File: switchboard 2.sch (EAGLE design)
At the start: 217 parts, among them IC1 MT8816AP, IC10 Z8F2480SO, IC11 LMV321M5, IC12 74HC595D, IC14 74LVC1G125DBV, IC15 74LVC1G125DBV, IC16 LM2940-9, IC17 PC817S OPTO, IC2 NE5532D, IC3 TC7660-SOIC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

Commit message: Polarity inversion protection diode added to -5V. USB ESD protection connection changed from GND to USB shield. Layout development and changes to improve performance, considering current loops.
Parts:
- added D20: LL4148, diode:DIODE-MINIMELF
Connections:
- net -5V: now also D20.A
- net GND: now also D20.C, H1.MOUNT, H2.MOUNT, H3.MOUNT; no longer D19.GND
- net USB_SHLD: now also D19.GND
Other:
- note added: "3.3V regulator as a option when FT232 (and its regulator) is not mounted or not used."
- note added: "Vin máx = 25 V"
- note removed: "3.3V regulator as a option when FT232 (and its regulator) is not mounted."
- moved on the sheet: C21, L1, SJ2

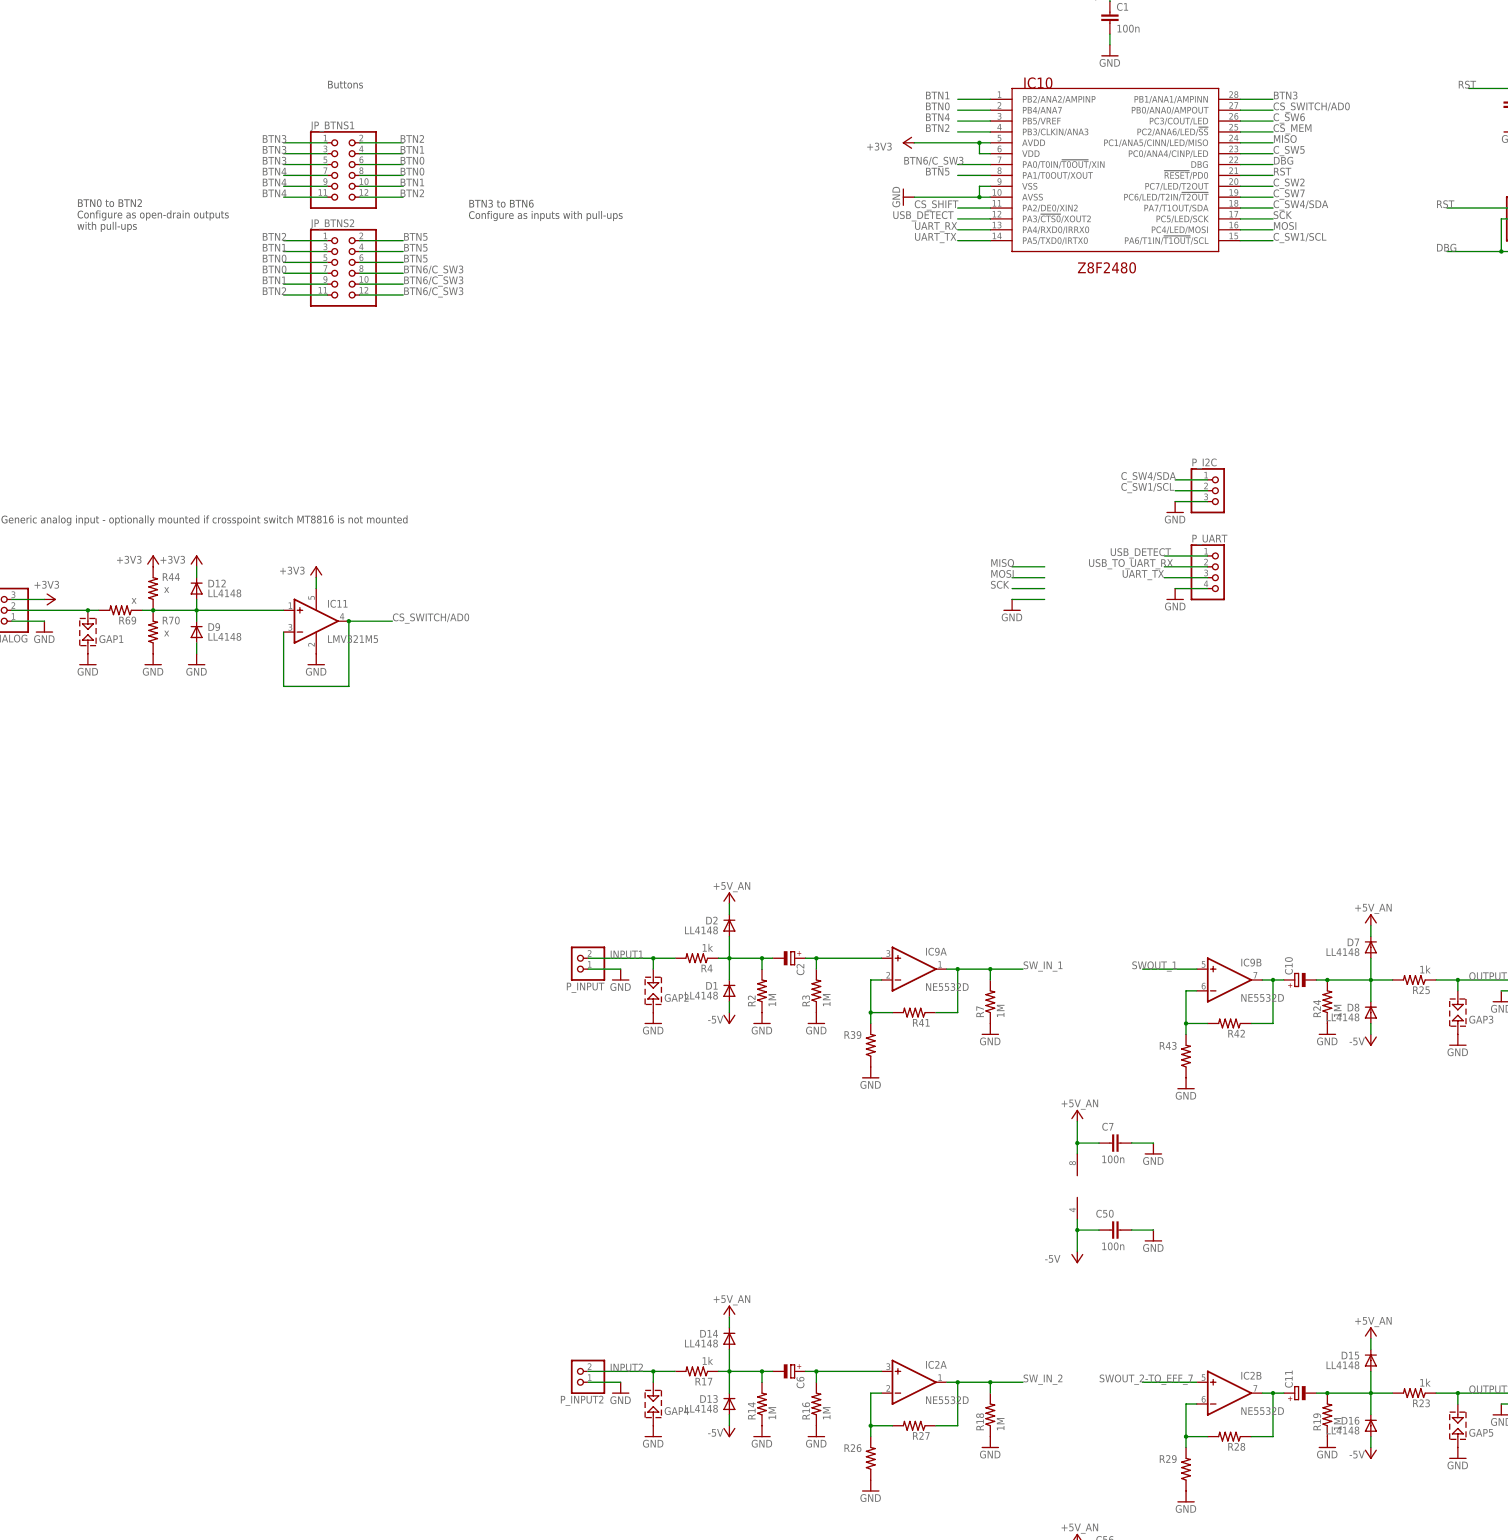
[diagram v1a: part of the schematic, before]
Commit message: Final adjustments to the schematic and layout. Cap added close to the generic input opamp. RC filter against EMI added to the audio inputs. Bias resistors added to output opamps.
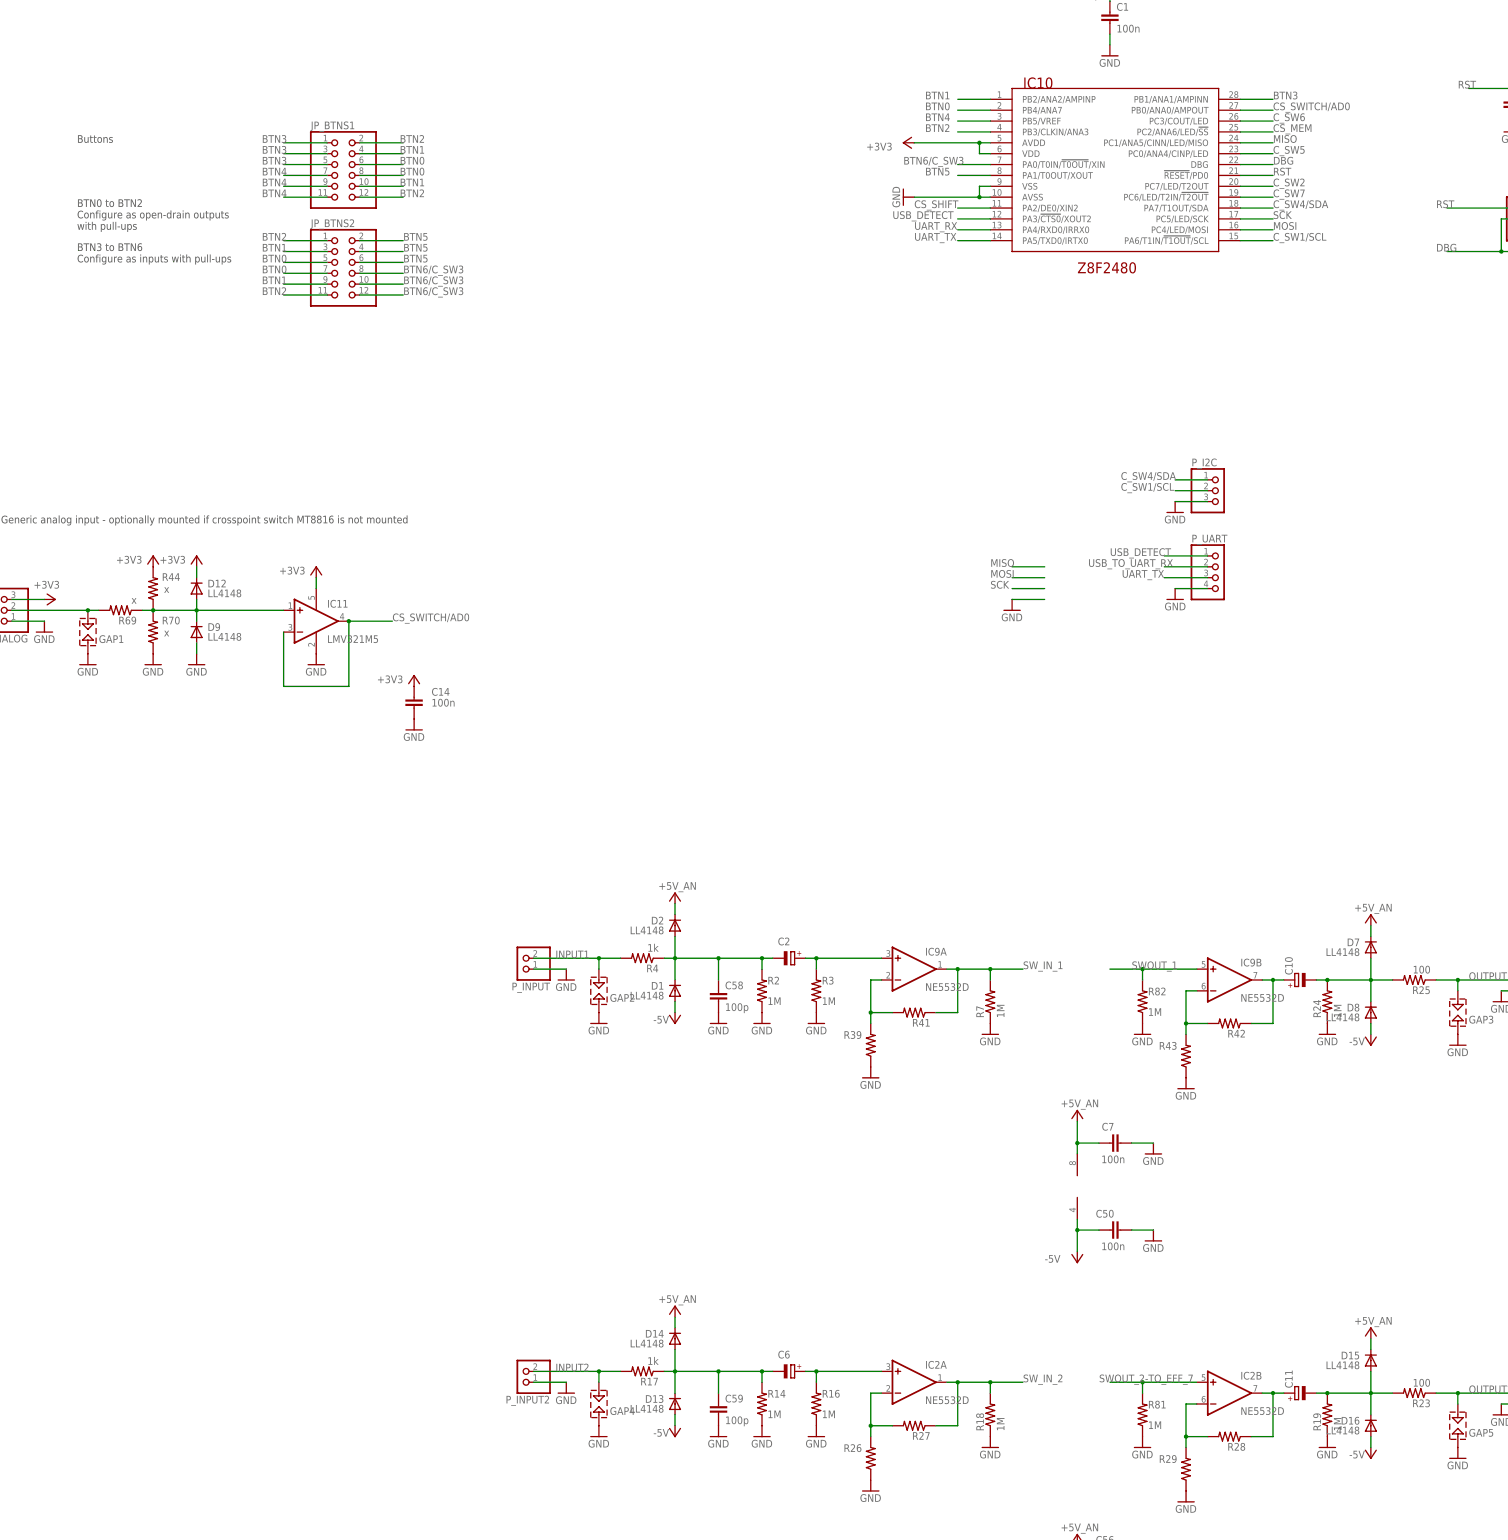
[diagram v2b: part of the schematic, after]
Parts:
- added C14: 100n, rcl:C-EUC0603
- added C58, C59: 100p, rcl:C-EUC0603
- added R81, R82: 1M, rcl:R-US_R0603
- R23, R25: value 1k -> 100
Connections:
- net +3V3: now also C14.1
- net GND: now also C14.2, C58.2, C59.2, R81.1, R82.1
- net N$4: now also C58.1
- net N$54: now also C59.1
- net SWOUT_1: now also R82.2
- net SWOUT_2-TO_EFF_7: now also R81.2
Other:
- moved on the sheet: D1, D13, D14, D2, GAP2, GAP4, P_INPUT, P_INPUT2, R17, R4

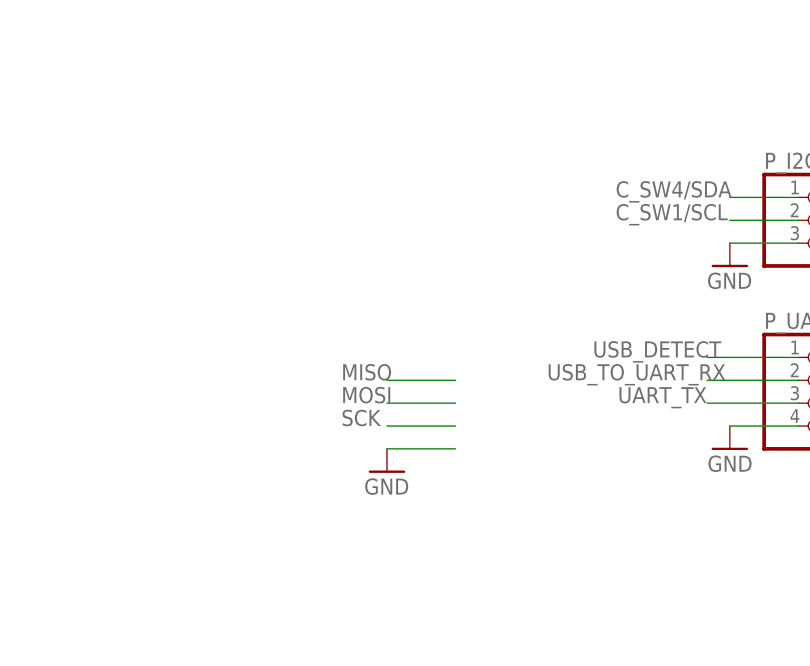
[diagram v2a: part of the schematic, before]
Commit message: Final adjustments. Test points added to SPI and supplies. PTSK Engineering text added (in solder mask stop layer).
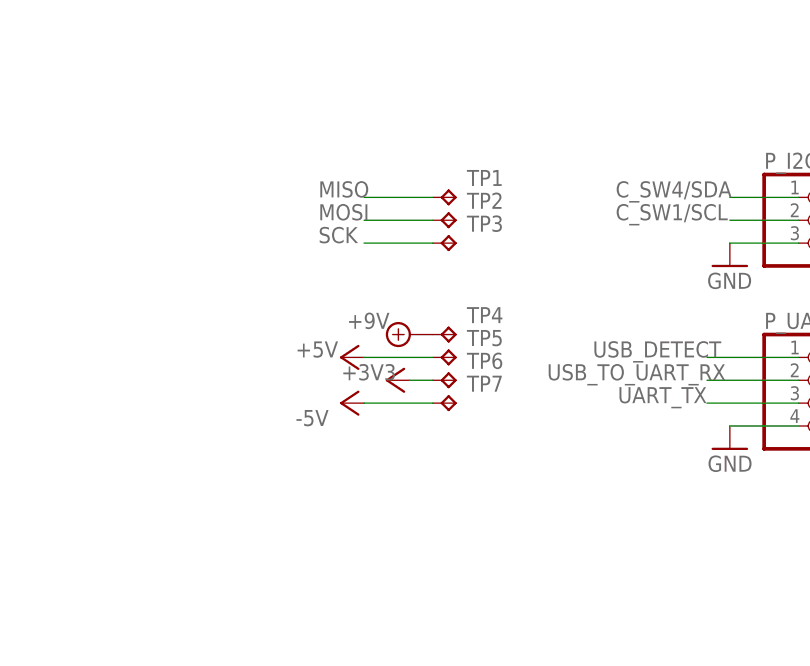
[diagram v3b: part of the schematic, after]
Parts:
- added TP1, TP2, TP3, TP4, TP5, TP6, TP7: TPB1,27, testpad:TPB1,27
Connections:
- net +3V3: now also TP6.TP
- net +5V: now also TP5.TP
- net +9V: now also TP4.TP
- net -5V: now also TP7.TP
- net MISO: now also TP1.TP
- net MOSI: now also TP2.TP
- net SCK: now also TP3.TP
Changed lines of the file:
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@@
 <part name="P_I2C" library="pinhead" deviceset="PINHD-1X3" device=""/>
 <part name="GND83" library="supply1" deviceset="GND" device=""/>
-<part name="GND85" library="supply1" deviceset="GND" device=""/>
 <part name="GAP6" library="PATSKO" deviceset="SPARK_GAP" device=""/>
 <part name="GND86" library="supply1" deviceset="GND" device=""/>
@@
 <part name="GND105" library="supply1" deviceset="GND" device=""/>
 <part name="GND106" library="supply1" deviceset="GND" device=""/>
+<part name="TP1" library="testpad" library_urn="urn:adsk.eagle:library:385" deviceset="TP" device="B1,27" package3d_urn="urn:adsk.eagle:package:27944/1"/>
+<part name="TP2" library="testpad" library_urn="urn:adsk.eagle:library:385" deviceset="TP" device="B1,27" package3d_urn="urn:adsk.eagle:package:27944/1"/>
+<part name="TP3" library="testpad" library_urn="urn:adsk.eagle:library:385" deviceset="TP" device="B1,27" package3d_urn="urn:adsk.eagle:package:27944/1"/>
+<part name="TP4" library="testpad" library_urn="urn:adsk.eagle:library:385" deviceset="TP" device="B1,27" package3d_urn="urn:adsk.eagle:package:27944/1"/>
+<part name="TP5" library="testpad" library_urn="urn:adsk.eagle:library:385" deviceset="TP" device="B1,27" package3d_urn="urn:adsk.eagle:package:27944/1"/>
+<part name="TP6" library="testpad" library_urn="urn:adsk.eagle:library:385" deviceset="TP" device="B1,27" package3d_urn="urn:adsk.eagle:package:27944/1"/>
+<part name="TP7" library="testpad" library_urn="urn:adsk.eagle:library:385" deviceset="TP" device="B1,27" package3d_urn="urn:adsk.eagle:package:27944/1"/>
+<part name="SUPPLY11" library="supply2" deviceset="+9V" device=""/>
+<part name="P+5" library="supply1" deviceset="+5V" device=""/>
+<part name="+3V9" library="supply1" deviceset="+3V3" device=""/>
+<part name="P-10" library="supply1" deviceset="-5V" device=""/>
 </parts>
 <sheets>
@@
 <instance part="P_I2C" gate="A" x="111.76" y="-22.86"/>
 <instance part="GND83" gate="1" x="101.6" y="-27.94"/>
-<instance part="GND85" gate="1" x="63.5" y="-50.8"/>
 <instance part="GAP6" gate="G$1" x="5.08" y="213.36"/>
 <instance part="GND86" gate="1" x="5.08" y="205.74"/>
@@
 <instance part="GND105" gate="1" x="93.98" y="-246.38"/>
 <instance part="GND106" gate="1" x="93.98" y="-149.86"/>
+<instance part="TP1" gate="G$1" x="71.12" y="-20.32" smashed="yes" rot="R270">
+<attribute name="NAME" x="72.39" y="-19.05" size="1.778" layer="95"/>
+<attribute name="TP_SIGNAL_NAME" x="69.85" y="-21.59" size="1.778" layer="97" rot="R270"/>
+</instance>
+<instance part="TP2" gate="G$1" x="71.12" y="-22.86" smashed="yes" rot="R270">
+<attribute name="NAME" x="72.39" y="-21.59" size="1.778" layer="95"/>
+<attribute name="TP_SIGNAL_NAME" x="69.85" y="-24.13" size="1.778" layer="97" rot="R270"/>
+</instance>
+<instance part="TP3" gate="G$1" x="71.12" y="-25.4" smashed="yes" rot="R270">
+<attribute name="NAME" x="72.39" y="-24.13" size="1.778" layer="95"/>
+<attribute name="TP_SIGNAL_NAME" x="69.85" y="-26.67" size="1.778" layer="97" rot="R270"/>
+</instance>
+<instance part="TP4" gate="G$1" x="71.12" y="-35.56" smashed="yes" rot="R270">
+<attribute name="NAME" x="72.39" y="-34.29" size="1.778" layer="95"/>
+<attribute name="TP_SIGNAL_NAME" x="69.85" y="-36.83" size="1.778" layer="97" rot="R270"/>
+</instance>
+<instance part="TP5" gate="G$1" x="71.12" y="-38.1" smashed="yes" rot="R270">
+<attribute name="NAME" x="72.39" y="-36.83" size="1.778" layer="95"/>
+<attribute name="TP_SIGNAL_NAME" x="69.85" y="-39.37" size="1.778" layer="97" rot="R270"/>
+</instance>
+<instance part="TP6" gate="G$1" x="71.12" y="-40.64" smashed="yes" rot="R270">
+<attribute name="NAME" x="72.39" y="-39.37" size="1.778" layer="95"/>
+<attribute name="TP_SIGNAL_NAME" x="69.85" y="-41.91" size="1.778" layer="97" rot="R270"/>
+</instance>
+<instance part="TP7" gate="G$1" x="71.12" y="-43.18" smashed="yes" rot="R270">
+<attribute name="NAME" x="72.39" y="-41.91" size="1.778" layer="95"/>
+<attribute name="TP_SIGNAL_NAME" x="69.85" y="-44.45" size="1.778" layer="97" rot="R270"/>
+</instance>
+<instance part="SUPPLY11" gate="G$1" x="66.04" y="-35.56" smashed="yes" rot="R90">
+<attribute name="VALUE" x="59.055" y="-34.925" size="1.778" layer="96"/>
+</instance>
+<instance part="P+5" gate="1" x="58.42" y="-38.1" smashed="yes" rot="R90">
+<attribute name="VALUE" x="53.34" y="-38.1" size="1.778" layer="96"/>
+</instance>
+<instance part="+3V9" gate="G$1" x="63.5" y="-40.64" smashed="yes" rot="R90">
+<attribute name="VALUE" x="58.42" y="-40.64" size="1.778" layer="96"/>
+</instance>
+<instance part="P-10" gate="1" x="58.42" y="-43.18" smashed="yes" rot="R270">
+<attribute name="VALUE" x="53.34" y="-45.72" size="1.778" layer="96"/>
+</instance>
 </instances>
 <busses>
@@
 <pinref part="+3V8" gate="G$1" pin="+3V3"/>
 </segment>
+<segment>
+<pinref part="TP6" gate="G$1" pin="TP"/>
+<pinref part="+3V9" gate="G$1" pin="+3V3"/>
+<wire x1="66.04" y1="-40.64" x2="68.58" y2="-40.64" width="0.1524" layer="91"/>
+</segment>
 </net>
 <net name="GND" class="0">
@@
 </segment>
 <segment>
-<wire x1="71.12" y1="-48.26" x2="63.5" y2="-48.26" width="0.1524" layer="91"/>
-<pinref part="GND85" gate="1" pin="GND"/>
-</segment>
-<segment>
 <pinref part="GAP6" gate="G$1" pin="2"/>
 <pinref part="GND86" gate="1" pin="GND"/>
@@
 <junction x="-340.36" y="137.16"/>
 </segment>
+<segment>
+<pinref part="TP5" gate="G$1" pin="TP"/>
+<pinref part="P+5" gate="1" pin="+5V"/>
+<wire x1="60.96" y1="-38.1" x2="68.58" y2="-38.1" width="0.1524" layer="91"/>
+</segment>
 </net>
 <net name="C_SW2" class="0">
@@
 </segment>
 <segment>
-<wire x1="71.12" y1="-43.18" x2="63.5" y2="-43.18" width="0.1524" layer="91"/>
-<label x="58.42" y="-43.18" size="1.778" layer="95"/>
+<wire x1="68.58" y1="-22.86" x2="60.96" y2="-22.86" width="0.1524" layer="91"/>
+<label x="55.88" y="-22.86" size="1.778" layer="95"/>
+<pinref part="TP2" gate="G$1" pin="TP"/>
 </segment>
 <segment>
@@
 </segment>
 <segment>
-<wire x1="71.12" y1="-40.64" x2="63.5" y2="-40.64" width="0.1524" layer="91"/>
-<label x="58.42" y="-40.64" size="1.778" layer="95"/>
+<wire x1="68.58" y1="-20.32" x2="60.96" y2="-20.32" width="0.1524" layer="91"/>
+<label x="55.88" y="-20.32" size="1.778" layer="95"/>
+<pinref part="TP1" gate="G$1" pin="TP"/>
 </segment>
 </net>
@@
 </segment>
 <segment>
-<wire x1="71.12" y1="-45.72" x2="63.5" y2="-45.72" width="0.1524" layer="91"/>
-<label x="58.42" y="-45.72" size="1.778" layer="95"/>
+<wire x1="68.58" y1="-25.4" x2="60.96" y2="-25.4" width="0.1524" layer="91"/>
+<label x="55.88" y="-25.4" size="1.778" layer="95"/>
+<pinref part="TP3" gate="G$1" pin="TP"/>
 </segment>
 <segment>
@@
 <pinref part="P-9" gate="1" pin="-5V"/>
 </segment>
+<segment>
+<pinref part="TP7" gate="G$1" pin="TP"/>
+<pinref part="P-10" gate="1" pin="-5V"/>
+<wire x1="60.96" y1="-43.18" x2="68.58" y2="-43.18" width="0.1524" layer="91"/>
+</segment>
 </net>
 <net name="C_SW4/SDA" class="0">
@@
 <pinref part="SUPPLY10" gate="G$1" pin="+9V"/>
 </segment>
+<segment>
+<pinref part="TP4" gate="G$1" pin="TP"/>
+<pinref part="SUPPLY11" gate="G$1" pin="+9V"/>
+</segment>
 </net>
